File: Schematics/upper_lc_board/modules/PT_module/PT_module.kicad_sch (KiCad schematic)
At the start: 5 parts, among them J4 PT1

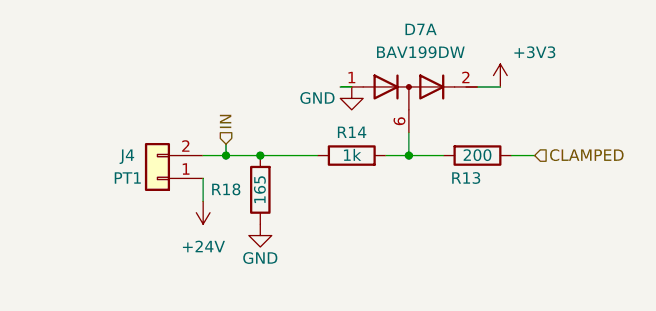
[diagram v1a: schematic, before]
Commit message: add references to caps, ferrite bead footprint, LDO datasheet
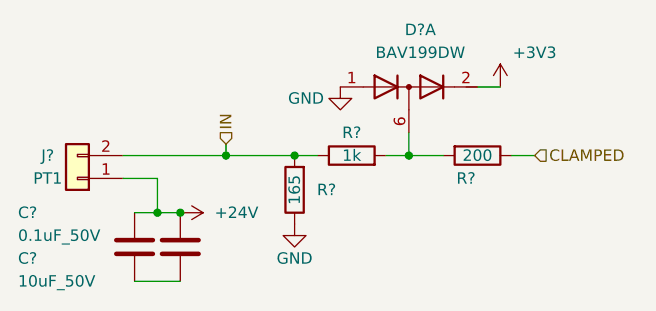
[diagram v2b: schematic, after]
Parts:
- removed R13: 200, Resistor_SMD:R_0603_1608Metric, symbol Device:R
- removed R14: 1k, Resistor_SMD:R_1206_3216Metric_Pad1.30x1.75mm_HandSolder, symbol Device:R
- added C?: 0.1uF_50V, Capacitor_SMD:C_0805_2012Metric, symbol Device:C
- added C?: 10uF_50V, Capacitor_SMD:C_1206_3216Metric, symbol Device:C
- added R?: 200, Resistor_SMD:R_0603_1608Metric, symbol Device:R
- added R?: 1k, Resistor_SMD:R_1206_3216Metric_Pad1.30x1.75mm_HandSolder, symbol Device:R
- renumbered D7 to D?, J4 to J?, R18 to R?
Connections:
- net +24V: now also C?.1, C?.1
- net CLAMPED: now also R?.1
- net IN: now also R?.1
- net at D?.6 (K3A4): now also R?.2, R?.2
- new net: C?.2, C?.2
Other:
- moved on the sheet: J?, R?
